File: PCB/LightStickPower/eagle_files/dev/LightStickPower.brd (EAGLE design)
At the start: 25 x 18 mm, 7 parts

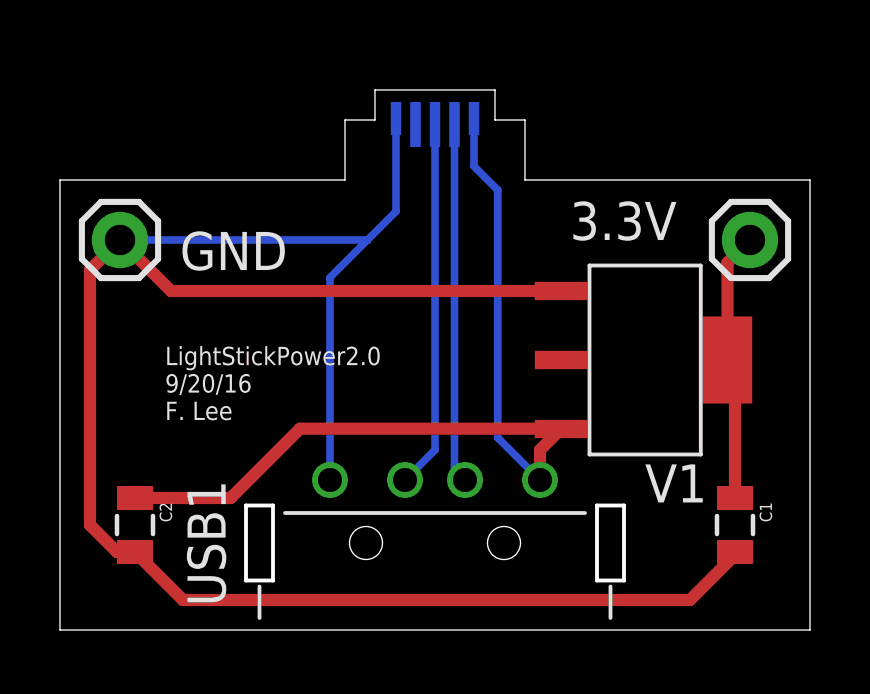
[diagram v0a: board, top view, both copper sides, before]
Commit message: Narrow board to fit in tube.
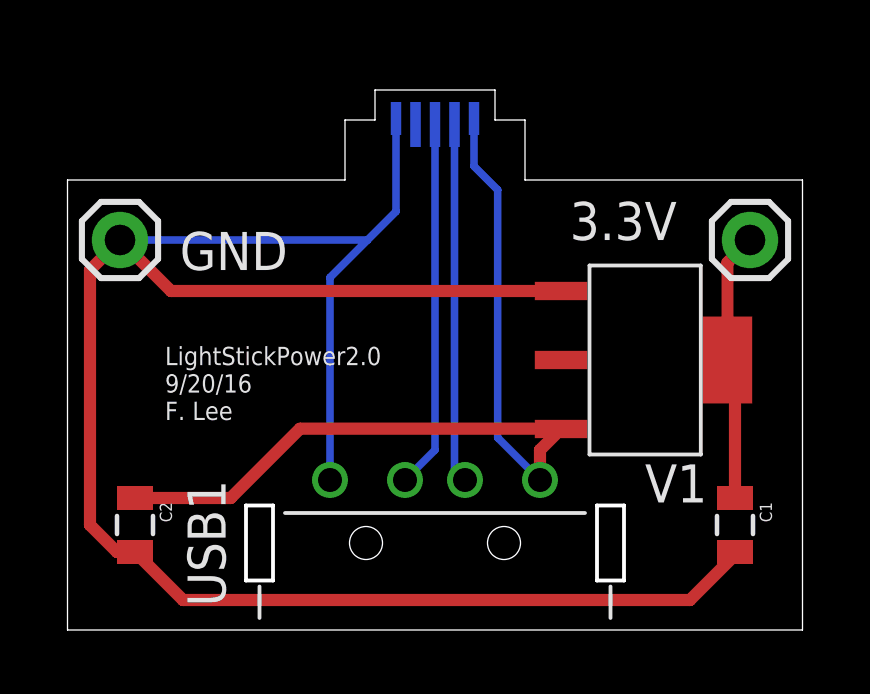
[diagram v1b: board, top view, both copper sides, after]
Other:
- board size 25 x 18 mm -> 24.5 x 18 mm
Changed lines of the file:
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@@
 <board>
 <plain>
-<wire x1="0" y1="0" x2="25" y2="0" width="0" layer="20"/>
-<wire x1="25" y1="0" x2="25" y2="15" width="0" layer="20"/>
-<wire x1="0" y1="15" x2="0" y2="0" width="0" layer="20"/>
-<wire x1="0" y1="15" x2="9.5" y2="15" width="0" layer="20"/>
-<wire x1="25" y1="15" x2="15.5" y2="15" width="0" layer="20"/>
+<wire x1="0.25" y1="0" x2="24.75" y2="0" width="0" layer="20"/>
+<wire x1="24.75" y1="0" x2="24.75" y2="15" width="0" layer="20"/>
+<wire x1="0.25" y1="15" x2="0.25" y2="0" width="0" layer="20"/>
+<wire x1="0.25" y1="15" x2="9.5" y2="15" width="0" layer="20"/>
+<wire x1="24.75" y1="15" x2="15.5" y2="15" width="0" layer="20"/>
 <wire x1="15.5" y1="15" x2="15.5" y2="17" width="0" layer="20"/>
 <wire x1="9.5" y1="17" x2="9.5" y2="15" width="0" layer="20"/>

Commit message: Adjust USB micro B head of LightStickPower.
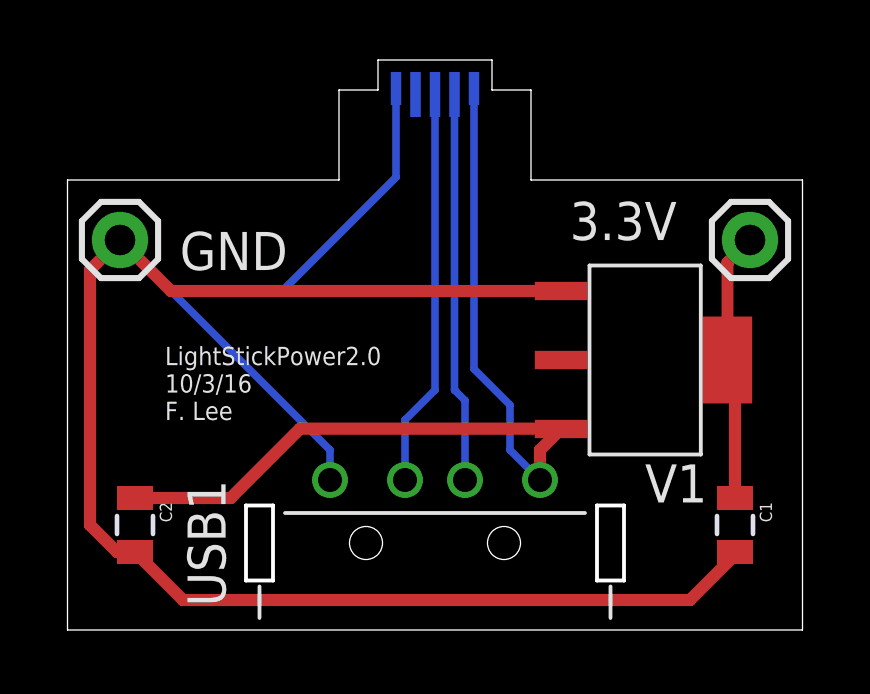
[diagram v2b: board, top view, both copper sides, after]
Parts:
- moved USB2 1.00 mm to (12.5, 18.6)
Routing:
- net N$5: track 69.8 -> 71.5 mm
- net N$3: track 12.3 -> 13.3 mm
- net N$2: track 12.0 -> 13.0 mm
- net N$1: track 30.1 -> 31.1 mm
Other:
- board size 24.5 x 18 mm -> 24.5 x 19 mm
- board text added: "LightStickPower2.0 10/3/16 F. Lee"
- board text removed: "LightStickPower2.0 9/20/16 F. Lee"
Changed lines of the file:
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@@
 <wire x1="24.75" y1="0" x2="24.75" y2="15" width="0" layer="20"/>
 <wire x1="0.25" y1="15" x2="0.25" y2="0" width="0" layer="20"/>
-<wire x1="0.25" y1="15" x2="9.5" y2="15" width="0" layer="20"/>
-<wire x1="24.75" y1="15" x2="15.5" y2="15" width="0" layer="20"/>
-<wire x1="15.5" y1="15" x2="15.5" y2="17" width="0" layer="20"/>
-<wire x1="9.5" y1="17" x2="9.5" y2="15" width="0" layer="20"/>
+<wire x1="0.25" y1="15" x2="9.3" y2="15" width="0" layer="20"/>
+<wire x1="24.75" y1="15" x2="15.7" y2="15" width="0" layer="20"/>
+<wire x1="15.7" y1="15" x2="15.7" y2="18" width="0" layer="20"/>
+<wire x1="9.3" y1="18" x2="9.3" y2="15" width="0" layer="20"/>
 <text x="3.5" y="7" size="0.6096" layer="25">LightStickPower2.0
-9/20/16
+10/3/16
 F. Lee</text>
-<wire x1="9.5" y1="17" x2="10.5" y2="17" width="0" layer="20"/>
-<wire x1="10.5" y1="17" x2="10.5" y2="18" width="0" layer="20"/>
-<wire x1="10.5" y1="18" x2="14.5" y2="18" width="0" layer="20"/>
-<wire x1="14.5" y1="18" x2="14.5" y2="17" width="0" layer="20"/>
-<wire x1="14.5" y1="17" x2="15.5" y2="17" width="0" layer="20"/>
+<wire x1="9.3" y1="18" x2="10.6" y2="18" width="0" layer="20"/>
+<wire x1="10.6" y1="18" x2="10.6" y2="19" width="0" layer="20"/>
+<wire x1="10.6" y1="19" x2="14.4" y2="19" width="0" layer="20"/>
+<wire x1="14.4" y1="19" x2="14.4" y2="18" width="0" layer="20"/>
+<wire x1="14.4" y1="18" x2="15.7" y2="18" width="0" layer="20"/>
 </plain>
 <attributes>
@@
 <attribute name="NAME" x="4.25" y="5" size="1.27" layer="25" rot="R270"/>
 </element>
-<element name="USB2" library="freddyLibr" package="USB_MICROB_PLUG_ZX64_B_5S" value="USB_MICROB_PLUG_ZX64_B_5S" x="12.5" y="17.6" smashed="yes" rot="MR180">
-<attribute name="NAME" x="10.55" y="14.79" size="1.27" layer="26" rot="MR180"/>
+<element name="USB2" library="freddyLibr" package="USB_MICROB_PLUG_ZX64_B_5S" value="USB_MICROB_PLUG_ZX64_B_5S" x="12.5" y="18.6" smashed="yes" rot="MR180">
+<attribute name="NAME" x="10.55" y="15.79" size="1.27" layer="26" rot="MR180"/>
 </element>
 <element name="GND" library="SparkFun-Connectors" package="1X01" value="" x="2" y="13" smashed="yes">
@@
 <wire x1="16" y1="5" x2="16" y2="6" width="0.4064" layer="1"/>
 <wire x1="16" y1="6" x2="16.7" y2="6.7" width="0.4064" layer="1"/>
-<wire x1="13.8" y1="17.05" x2="13.8" y2="15.46" width="0.254" layer="16"/>
-<wire x1="13.8" y1="15.46" x2="14.59" y2="14.67" width="0.254" layer="16"/>
-<wire x1="14.59" y1="14.67" x2="14.59" y2="6.41" width="0.254" layer="16"/>
-<wire x1="14.59" y1="6.41" x2="16" y2="5" width="0.254" layer="16"/>
+<wire x1="13.8" y1="18.05" x2="13.8" y2="8.7" width="0.254" layer="16"/>
+<wire x1="13.8" y1="8.7" x2="15" y2="7.5" width="0.254" layer="16"/>
+<wire x1="15" y1="7.5" x2="15" y2="6" width="0.254" layer="16"/>
+<wire x1="15" y1="6" x2="16" y2="5" width="0.254" layer="16"/>
 </signal>
 <signal name="N$2">
 <contactref element="USB1" pad="D-"/>
 <contactref element="USB2" pad="DATA-"/>
-<wire x1="13.15" y1="16.85" x2="13.15" y2="5.35" width="0.254" layer="16"/>
-<wire x1="13.15" y1="5.35" x2="13.5" y2="5" width="0.254" layer="16"/>
+<wire x1="13.5" y1="5" x2="13.5" y2="7.65" width="0.254" layer="16"/>
+<wire x1="13.5" y1="7.65" x2="13.15" y2="8" width="0.254" layer="16"/>
+<wire x1="13.15" y1="8" x2="13.15" y2="17.85" width="0.254" layer="16"/>
 </signal>
 <signal name="N$3">
 <contactref element="USB1" pad="D+"/>
 <contactref element="USB2" pad="DATA+"/>
-<wire x1="12.5" y1="16.85" x2="12.5" y2="6" width="0.254" layer="16"/>
-<wire x1="12.5" y1="6" x2="11.5" y2="5" width="0.254" layer="16"/>
+<wire x1="12.5" y1="17.85" x2="12.5" y2="8" width="0.254" layer="16"/>
+<wire x1="12.5" y1="8" x2="11.5" y2="7" width="0.254" layer="16"/>
+<wire x1="11.5" y1="7" x2="11.5" y2="5" width="0.254" layer="16"/>
 </signal>
 <signal name="N$7">
@@
 <contactref element="USB2" pad="GND"/>
 <contactref element="V1" pad="GND"/>
-<wire x1="2" y1="13" x2="10.25" y2="13" width="0.254" layer="16"/>
-<wire x1="9" y1="5" x2="9" y2="11.75" width="0.254" layer="16"/>
-<wire x1="9" y1="11.75" x2="10.25" y2="13" width="0.254" layer="16"/>
 <wire x1="2.5" y1="2.6" x2="1.9" y2="2.6" width="0.4064" layer="1"/>
 <wire x1="1.9" y1="2.6" x2="1" y2="3.5" width="0.4064" layer="1"/>
@@
 <wire x1="21" y1="1" x2="4.1" y2="1" width="0.4064" layer="1"/>
 <wire x1="4.1" y1="1" x2="2.5" y2="2.6" width="0.4064" layer="1"/>
-<wire x1="11.2" y1="17.05" x2="11.2" y2="13.95" width="0.254" layer="16"/>
-<wire x1="11.2" y1="13.95" x2="10.25" y2="13" width="0.254" layer="16"/>
+<wire x1="9" y1="5" x2="9" y2="6" width="0.254" layer="16"/>
+<wire x1="9" y1="6" x2="3.73" y2="11.27" width="0.254" layer="16"/>
+<wire x1="3.73" y1="11.27" x2="2" y2="13" width="0.254" layer="16"/>
+<wire x1="11.2" y1="18.05" x2="11.2" y2="15.09" width="0.254" layer="16"/>
+<wire x1="11.2" y1="15.09" x2="7.41" y2="11.3" width="0.254" layer="16"/>
+<wire x1="7.41" y1="11.3" x2="3.76" y2="11.3" width="0.254" layer="16"/>
+<wire x1="3.76" y1="11.3" x2="3.73" y2="11.27" width="0.254" layer="16"/>
 </signal>
 </signals>

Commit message: Updated Light stick power to use cabled USB-micro-B plug. Also commit properly pathed copy_eagle. Getting annoying.
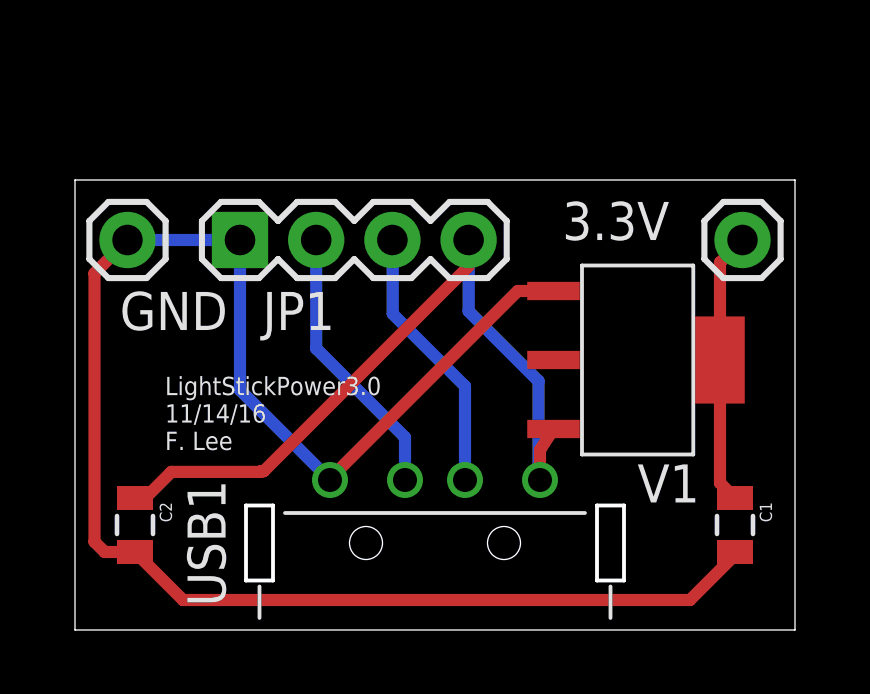
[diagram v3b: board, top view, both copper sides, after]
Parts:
- removed USB2: USB_MICROB_PLUG_ZX64_B_5S, freddyLibr:USB_MICROB_PLUG_ZX64_B_5S
- added JP1: (no value), SparkFun-Connectors:1X04
- moved 3.3V 0.25 mm to (22.8, 13.0)
- moved GND 0.25 mm to (2.25, 13.0)
- moved V1 0.25 mm to (19.2, 9.00)
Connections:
- net N$1: now also JP1.4; no longer USB2.VCC
- net N$2: now also JP1.3; no longer USB2.DATA-
- net N$3: now also JP1.2; no longer USB2.DATA+
- net N$5: now also JP1.1; no longer USB2.GND
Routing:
- net N$5: track 71.5 -> 56.5 mm
- net N$1: track 31.1 -> 26.0 mm
- net N$3: track 13.3 -> 9.23 mm
- net N$2: track 13.0 -> 9.00 mm
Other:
- board size 24.5 x 19 mm -> 24 x 15 mm
- board text added: "LightStickPower3.0 11/14/16 F. Lee"
- board text removed: "LightStickPower2.0 10/3/16 F. Lee"
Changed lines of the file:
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@@
 <board>
 <plain>
-<wire x1="0.25" y1="0" x2="24.75" y2="0" width="0" layer="20"/>
-<wire x1="24.75" y1="0" x2="24.75" y2="15" width="0" layer="20"/>
-<wire x1="0.25" y1="15" x2="0.25" y2="0" width="0" layer="20"/>
-<wire x1="0.25" y1="15" x2="9.3" y2="15" width="0" layer="20"/>
-<wire x1="24.75" y1="15" x2="15.7" y2="15" width="0" layer="20"/>
-<wire x1="15.7" y1="15" x2="15.7" y2="18" width="0" layer="20"/>
-<wire x1="9.3" y1="18" x2="9.3" y2="15" width="0" layer="20"/>
-<text x="3.5" y="7" size="0.6096" layer="25">LightStickPower2.0
-10/3/16
+<wire x1="0.5" y1="0" x2="24.5" y2="0" width="0" layer="20"/>
+<wire x1="24.5" y1="0" x2="24.5" y2="15" width="0" layer="20"/>
+<wire x1="0.5" y1="15" x2="0.5" y2="0" width="0" layer="20"/>
+<wire x1="24.5" y1="15" x2="0.5" y2="15" width="0" layer="20"/>
+<text x="3.5" y="6" size="0.6096" layer="25">LightStickPower3.0
+11/14/16
 F. Lee</text>
-<wire x1="9.3" y1="18" x2="10.6" y2="18" width="0" layer="20"/>
-<wire x1="10.6" y1="18" x2="10.6" y2="19" width="0" layer="20"/>
-<wire x1="10.6" y1="19" x2="14.4" y2="19" width="0" layer="20"/>
-<wire x1="14.4" y1="19" x2="14.4" y2="18" width="0" layer="20"/>
-<wire x1="14.4" y1="18" x2="15.7" y2="18" width="0" layer="20"/>
 </plain>
 <attributes>
@@
 <attribute name="NAME" x="4.25" y="5" size="1.27" layer="25" rot="R270"/>
 </element>
-<element name="USB2" library="freddyLibr" package="USB_MICROB_PLUG_ZX64_B_5S" value="USB_MICROB_PLUG_ZX64_B_5S" x="12.5" y="18.6" smashed="yes" rot="MR180">
-<attribute name="NAME" x="10.55" y="15.79" size="1.27" layer="26" rot="MR180"/>
-</element>
-<element name="GND" library="SparkFun-Connectors" package="1X01" value="" x="2" y="13" smashed="yes">
-<attribute name="NAME" x="3.9938" y="11.9988" size="1.27" layer="25"/>
-<attribute name="VALUE" x="0.73" y="9.825" size="1.27" layer="27"/>
-</element>
-<element name="3.3V" library="SparkFun-Connectors" package="1X01" value="" x="23" y="13" smashed="yes">
-<attribute name="NAME" x="16.9938" y="12.9988" size="1.27" layer="25"/>
-<attribute name="VALUE" x="21.73" y="9.825" size="1.27" layer="27"/>
+<element name="GND" library="SparkFun-Connectors" package="1X01" value="" x="2.25" y="13" smashed="yes">
+<attribute name="NAME" x="1.9938" y="9.9988" size="1.27" layer="25"/>
+<attribute name="VALUE" x="0.98" y="9.825" size="1.27" layer="27"/>
+</element>
+<element name="3.3V" library="SparkFun-Connectors" package="1X01" value="" x="22.75" y="13" smashed="yes">
+<attribute name="NAME" x="16.7438" y="12.9988" size="1.27" layer="25"/>
+<attribute name="VALUE" x="21.48" y="9.825" size="1.27" layer="27"/>
 </element>
 <element name="C1" library="SparkFun-Capacitors" package="0805" value="" x="22.5" y="3.5" smashed="yes" rot="R270">
@@
 <attribute name="VALUE" x="1.103" y="4.516" size="0.4064" layer="27" rot="R270"/>
 </element>
-<element name="V1" library="freddyLibr" package="SOT-223" value="VOLTAGE_REGULATOR_AP2114H" x="19.5" y="9" smashed="yes" rot="R270">
-<attribute name="NAME" x="19.5" y="4.25" size="1.27" layer="25"/>
+<element name="V1" library="freddyLibr" package="SOT-223" value="VOLTAGE_REGULATOR_AP2114H" x="19.25" y="9" smashed="yes" rot="R270">
+<attribute name="NAME" x="19.25" y="4.25" size="1.27" layer="25"/>
+</element>
+<element name="JP1" library="SparkFun-Connectors" package="1X04" value="" x="6" y="13" smashed="yes">
+<attribute name="NAME" x="6.7538" y="9.9988" size="1.27" layer="25" ratio="10"/>
+<attribute name="VALUE" x="4.73" y="9.825" size="1.27" layer="27"/>
 </element>
 </elements>
@@
 <signal name="N$1">
 <contactref element="USB1" pad="VCC"/>
-<contactref element="USB2" pad="VCC"/>
 <contactref element="C2" pad="1"/>
 <contactref element="V1" pad="VIN"/>
-<wire x1="2.5" y1="4.4" x2="5.69" y2="4.4" width="0.4064" layer="1"/>
-<wire x1="5.69" y1="4.4" x2="8" y2="6.71" width="0.4064" layer="1"/>
-<wire x1="8" y1="6.71" x2="16.69" y2="6.71" width="0.4064" layer="1"/>
-<wire x1="16.69" y1="6.71" x2="16.7" y2="6.7" width="0.4064" layer="1"/>
 <wire x1="16" y1="5" x2="16" y2="6" width="0.4064" layer="1"/>
-<wire x1="16" y1="6" x2="16.7" y2="6.7" width="0.4064" layer="1"/>
-<wire x1="13.8" y1="18.05" x2="13.8" y2="8.7" width="0.254" layer="16"/>
-<wire x1="13.8" y1="8.7" x2="15" y2="7.5" width="0.254" layer="16"/>
-<wire x1="15" y1="7.5" x2="15" y2="6" width="0.254" layer="16"/>
-<wire x1="15" y1="6" x2="16" y2="5" width="0.254" layer="16"/>
+<wire x1="16" y1="6" x2="16.45" y2="6.7" width="0.4064" layer="1"/>
+<contactref element="JP1" pad="4"/>
+<wire x1="13.62" y1="13" x2="13.62" y2="10.63" width="0.4064" layer="16"/>
+<wire x1="13.62" y1="10.63" x2="15.95" y2="8.3" width="0.4064" layer="16"/>
+<wire x1="15.95" y1="8.3" x2="15.95" y2="5.05" width="0.4064" layer="16"/>
+<wire x1="15.95" y1="5.05" x2="16" y2="5" width="0.4064" layer="16"/>
+<wire x1="2.5" y1="4.4" x2="2.84" y2="4.4" width="0.4064" layer="1"/>
+<wire x1="2.84" y1="4.4" x2="3.71" y2="5.27" width="0.4064" layer="1"/>
+<wire x1="3.71" y1="5.27" x2="6.67" y2="5.27" width="0.4064" layer="1"/>
+<wire x1="6.67" y1="5.27" x2="6.69" y2="5.29" width="0.4064" layer="1"/>
+<wire x1="6.69" y1="5.29" x2="6.79" y2="5.29" width="0.4064" layer="1"/>
+<wire x1="6.79" y1="5.29" x2="13.62" y2="12.12" width="0.4064" layer="1"/>
+<wire x1="13.62" y1="12.12" x2="13.62" y2="13" width="0.4064" layer="1"/>
 </signal>
 <signal name="N$2">
 <contactref element="USB1" pad="D-"/>
-<contactref element="USB2" pad="DATA-"/>
-<wire x1="13.5" y1="5" x2="13.5" y2="7.65" width="0.254" layer="16"/>
-<wire x1="13.5" y1="7.65" x2="13.15" y2="8" width="0.254" layer="16"/>
-<wire x1="13.15" y1="8" x2="13.15" y2="17.85" width="0.254" layer="16"/>
+<contactref element="JP1" pad="3"/>
+<wire x1="13.5" y1="5" x2="13.5" y2="8.13" width="0.4064" layer="16"/>
+<wire x1="13.5" y1="8.13" x2="11.09" y2="10.54" width="0.4064" layer="16"/>
+<wire x1="11.09" y1="10.54" x2="11.09" y2="12.99" width="0.4064" layer="16"/>
+<wire x1="11.09" y1="12.99" x2="11.08" y2="13" width="0.4064" layer="16"/>
 </signal>
 <signal name="N$3">
 <contactref element="USB1" pad="D+"/>
-<contactref element="USB2" pad="DATA+"/>
-<wire x1="12.5" y1="17.85" x2="12.5" y2="8" width="0.254" layer="16"/>
-<wire x1="12.5" y1="8" x2="11.5" y2="7" width="0.254" layer="16"/>
-<wire x1="11.5" y1="7" x2="11.5" y2="5" width="0.254" layer="16"/>
+<contactref element="JP1" pad="2"/>
+<wire x1="11.5" y1="5" x2="11.5" y2="6.42" width="0.4064" layer="16"/>
+<wire x1="11.5" y1="6.42" x2="8.54" y2="9.38" width="0.4064" layer="16"/>
+<wire x1="8.54" y1="9.38" x2="8.54" y2="13" width="0.4064" layer="16"/>
 </signal>
 <signal name="N$7">
@@
 <contactref element="C1" pad="1"/>
 <contactref element="V1" pad="VOUT2"/>
-<wire x1="22.5" y1="4.4" x2="22.5" y2="8.75" width="0.4064" layer="1"/>
-<wire x1="22.5" y1="8.75" x2="22.25" y2="9" width="0.4064" layer="1"/>
-<wire x1="22.25" y1="9" x2="22.25" y2="12.25" width="0.4064" layer="1"/>
-<wire x1="22.25" y1="12.25" x2="23" y2="13" width="0.4064" layer="1"/>
+<wire x1="22" y1="9" x2="22" y2="12.25" width="0.4064" layer="1"/>
+<wire x1="22" y1="12.25" x2="22.75" y2="13" width="0.4064" layer="1"/>
+<wire x1="22" y1="9" x2="22" y2="4.9" width="0.4064" layer="1"/>
+<wire x1="22" y1="4.9" x2="22.5" y2="4.4" width="0.4064" layer="1"/>
 </signal>
 <signal name="N$5">
@@
 <contactref element="USB1" pad="GND"/>
 <contactref element="GND" pad="1"/>
-<contactref element="USB2" pad="GND"/>
 <contactref element="V1" pad="GND"/>
-<wire x1="2.5" y1="2.6" x2="1.9" y2="2.6" width="0.4064" layer="1"/>
-<wire x1="1.9" y1="2.6" x2="1" y2="3.5" width="0.4064" layer="1"/>
-<wire x1="1" y1="3.5" x2="1" y2="12" width="0.4064" layer="1"/>
-<wire x1="1" y1="12" x2="2" y2="13" width="0.4064" layer="1"/>
-<wire x1="16.7" y1="11.3" x2="3.7" y2="11.3" width="0.4064" layer="1"/>
-<wire x1="3.7" y1="11.3" x2="2" y2="13" width="0.4064" layer="1"/>
 <wire x1="22.5" y1="2.6" x2="22.5" y2="2.5" width="0.4064" layer="1"/>
 <wire x1="22.5" y1="2.5" x2="21" y2="1" width="0.4064" layer="1"/>
 <wire x1="21" y1="1" x2="4.1" y2="1" width="0.4064" layer="1"/>
 <wire x1="4.1" y1="1" x2="2.5" y2="2.6" width="0.4064" layer="1"/>
-<wire x1="9" y1="5" x2="9" y2="6" width="0.254" layer="16"/>
-<wire x1="9" y1="6" x2="3.73" y2="11.27" width="0.254" layer="16"/>
-<wire x1="3.73" y1="11.27" x2="2" y2="13" width="0.254" layer="16"/>
-<wire x1="11.2" y1="18.05" x2="11.2" y2="15.09" width="0.254" layer="16"/>
-<wire x1="11.2" y1="15.09" x2="7.41" y2="11.3" width="0.254" layer="16"/>
-<wire x1="7.41" y1="11.3" x2="3.76" y2="11.3" width="0.254" layer="16"/>
-<wire x1="3.76" y1="11.3" x2="3.73" y2="11.27" width="0.254" layer="16"/>
+<contactref element="JP1" pad="1"/>
+<wire x1="2.25" y1="13" x2="2.25" y2="12.99" width="0.4064" layer="1"/>
+<wire x1="2.25" y1="12.99" x2="1.15" y2="11.89" width="0.4064" layer="1"/>
+<wire x1="1.15" y1="11.89" x2="1.15" y2="2.94" width="0.4064" layer="1"/>
+<wire x1="1.15" y1="2.94" x2="1.49" y2="2.6" width="0.4064" layer="1"/>
+<wire x1="1.49" y1="2.6" x2="2.5" y2="2.6" width="0.4064" layer="1"/>
+<wire x1="6" y1="13" x2="6" y2="8" width="0.4064" layer="16"/>
+<wire x1="6" y1="8" x2="9" y2="5" width="0.4064" layer="16"/>
+<wire x1="2.25" y1="13" x2="6" y2="13" width="0.4064" layer="16"/>
+<wire x1="9" y1="5" x2="9" y2="5.04" width="0.4064" layer="1"/>
+<wire x1="9" y1="5.04" x2="15.26" y2="11.3" width="0.4064" layer="1"/>
+<wire x1="15.26" y1="11.3" x2="16.45" y2="11.3" width="0.4064" layer="1"/>
 </signal>
 </signals>

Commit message: Move some elements around.
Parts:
- moved 3.3V 0.50 mm to (22.2, 13.0)
- moved C1 0.50 mm to (22.0, 3.50)
- moved C2 0.50 mm to (2.00, 3.50)
- moved GND 0.50 mm to (1.75, 13.0)
- moved JP1 0.50 mm to (5.50, 13.0)
- moved USB1 0.50 mm to (12.0, 2.90)
- moved V1 0.50 mm to (18.8, 9.00)
